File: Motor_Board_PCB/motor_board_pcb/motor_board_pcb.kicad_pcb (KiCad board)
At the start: 2 copper layers, 104.8 x 60.3 mm, 107 parts, among them J1 CAN_OUT, J11 CSP-USC16-TR, J2 Screw_Terminal_01x04, J3 Conn_01x02, J4 Screw_Terminal_01x14, J5 Screw_Terminal_01x04, J6 Conn_01x03, J8 Conn_01x02, SW1 SW_Push, U1 R7FA4M1AB3CFM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

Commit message: Motor Board Initial Layout
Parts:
- removed R7: 5.1k, Resistor_SMD:R_0603_1608Metric
- removed SW1: SW_Push, Button_Switch_SMD:SW_Push_1P1T_NO_6x6mm_H9.5mm
- removed TP1, TP4, TP6: TestPoint, TestPoint:TestPoint_Pad_D1.0mm
- added TP10: TestPoint, TestPoint:TestPoint_Pad_D1.0mm, F.Cu at (143.3, 89.7)
- added TP11: TestPoint, TestPoint:TestPoint_Pad_D1.0mm, F.Cu at (139.3, 89.7)
- added TP12: TestPoint, TestPoint:TestPoint_Pad_D1.0mm, F.Cu at (141.3, 89.7)
- added TP13: TestPoint, TestPoint:TestPoint_Pad_D1.0mm, F.Cu at (137.3, 89.7)
- added TP14: TestPoint, TestPoint:TestPoint_Pad_D1.0mm, F.Cu at (153.4, 76.8)
- added TP15: TestPoint, TestPoint:TestPoint_Pad_D1.0mm, F.Cu at (151.4, 76.8)
- added TP16: TestPoint, TestPoint:TestPoint_Pad_D1.0mm, F.Cu at (158.0, 72.8)
- added TP17: TestPoint, TestPoint:TestPoint_Pad_D1.0mm, F.Cu at (160.0, 72.8)
- C1, C4, C8, L1, L2, R22, R3: moved to F.Cu
- C31, R1, R10, R11, R13, R14, R15, R2, R30, R4, R8, R9, RV1: moved to B.Cu
- J4: value Screw_Terminal_01x14 -> Screw_Terminal_01x06; footprint Connector_PinHeader_2.54mm:PinHeader_1x14_P2.54mm_Vertical -> Connector_PinHeader_2.54mm:PinHeader_1x06_P2.54mm_Vertical
- R6: value 5.1k -> 10k
- moved J3 128.4 mm to (94.5, 65.5), turned to 180 degrees
- moved R33 122.6 mm to (135.2, 73.0), turned to 180 degrees
- moved R32 119.5 mm to (138.4, 77.8), turned to 180 degrees
- moved TP9 116.4 mm to (129.6, 83.0)
- moved R31 116.0 mm to (141.9, 74.6)
- moved R1 109.1 mm to (167.9, 69.0), turned to -90 degrees
- moved R2 101.7 mm to (173.3, 69.1), turned to -90 degrees
- moved J8 97.9 mm to (184.9, 65.3), turned to 180 degrees
- moved J6 97.8 mm to (154.2, 60.1), turned to 90 degrees
- moved TP8 90.5 mm to (174.0, 72.7)
- moved TP7 89.1 mm to (174.0, 74.9)
- moved TP2 81.0 mm to (181.7, 68.7)
- moved D11 78.1 mm to (181.8, 64.8), turned to -90 degrees
- moved J5 69.4 mm to (184.6, 101.0), turned to -90 degrees
- moved J1 49.8 mm to (95.3, 91.6), turned to 180 degrees
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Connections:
- J4 pad 2: D13 -> D5
- J4 pad 3: D12 -> D4
- J4 pad 4: D11 -> D3
- J4 pad 5: D10 -> D2
- J4 pad 6: D7 -> GND
- R31 pad 1: Net-(U4-MS1_AD0) -> Net-(U4-MS2_AD1)
- R6 pad 2: Net-(R6-Pad2) -> GND
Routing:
- net +5V: track 0.00 -> 242.7 mm, vias 0 -> 7
- net GND: track 0.00 -> 54.5 mm, vias 0 -> 53
- net +12V: track 0.00 -> 45.8 mm, vias 0 -> 14
- net D11: track 0.00 -> 42.4 mm, vias 0 -> 4
- net D12: track 0.00 -> 40.8 mm, vias 0 -> 2
- net D13: track 0.00 -> 39.6 mm, vias 0 -> 2
- net D10: track 0.00 -> 38.4 mm
- net BOOT: track 0.00 -> 33.4 mm, vias 0 -> 1
- net ~{RESET}: track 0.00 -> 32.5 mm, vias 0 -> 1
- net /Connectors/SHIELD2: track 0.00 -> 29.6 mm, vias 0 -> 1
- net Net-(D6-K): track 0.00 -> 29.5 mm, vias 0 -> 2
- net D7: track 0.00 -> 28.2 mm, vias 0 -> 2
- net Net-(D7-K): track 0.00 -> 27.8 mm, vias 0 -> 2
- net VUSB: track 0.00 -> 27.1 mm, vias 0 -> 1
- net D6: track 0.00 -> 27.0 mm, vias 0 -> 2
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- added copper zone on B.Cu, net +12V
- added copper zone on F.Cu, net +12V
- added copper zone on F.Cu, net +5V
- added copper zone on F.Cu, net -BATT
- added copper zone on F.Cu, net /Motor_Driver/OUTA1
- added copper zone on F.Cu, net /Motor_Driver/OUTA2
- added copper zone on F.Cu, net /Motor_Driver/OUTB1
- added copper zone on F.Cu, net /Motor_Driver/OUTB2
- added copper zone on B.Cu, net GND
- added copper zone on F.Cu, net GND
- added copper zone on F.Cu, net Net-(C27-Pad2)
- added copper zone on F.Cu, net Net-(C30-Pad2)
- added copper zone on F.Cu, net Net-(C32-Pad2)
- added copper zone on F.Cu, net Net-(U6-BST)
- added copper zone on F.Cu, net Net-(U6-SW)
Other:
- board size 104.8 x 60.3 mm -> 95 x 45 mm
- rule pad_to_mask_clearance: 0 -> 0.05
- board text added: "PWR"
- board text added: "RX"
- board text added: "SCK"
- board text added: "TX"

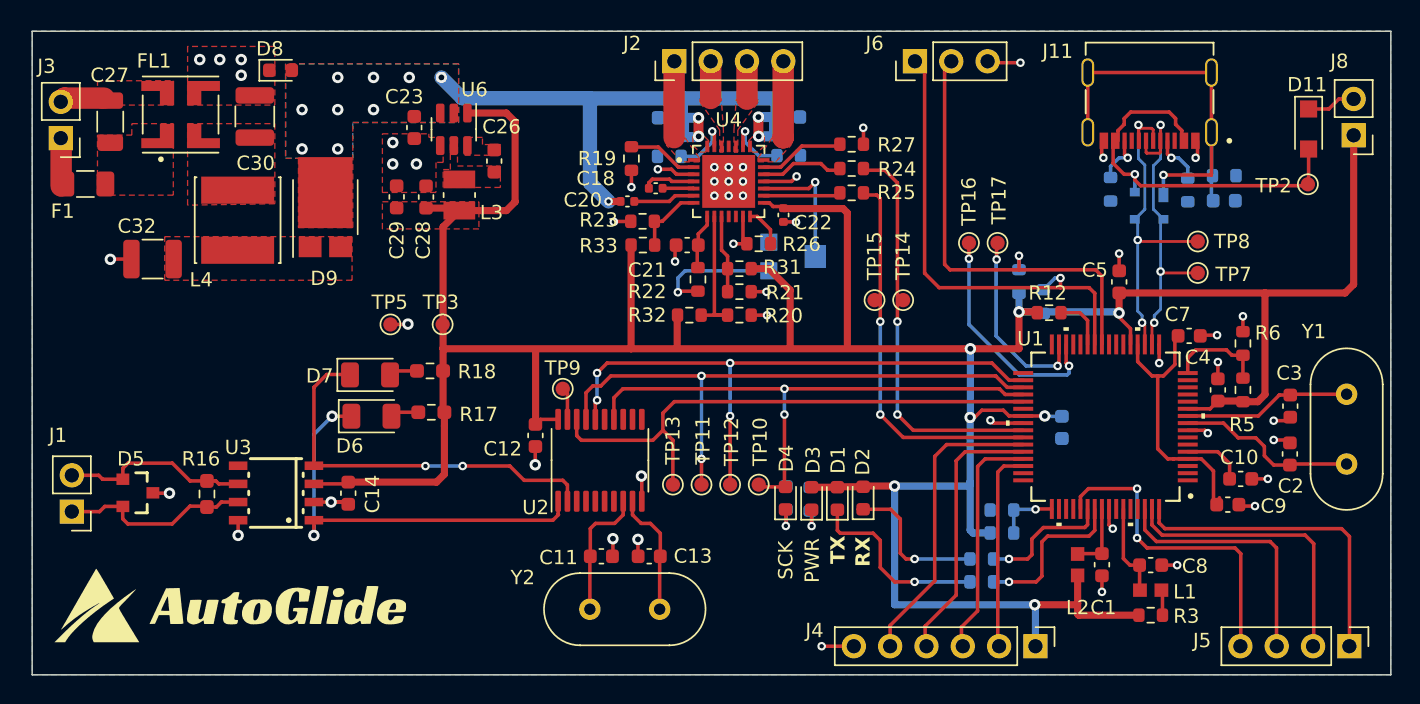
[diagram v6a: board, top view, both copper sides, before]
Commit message: Central hub layout first draft (+ some changes to motor driver)
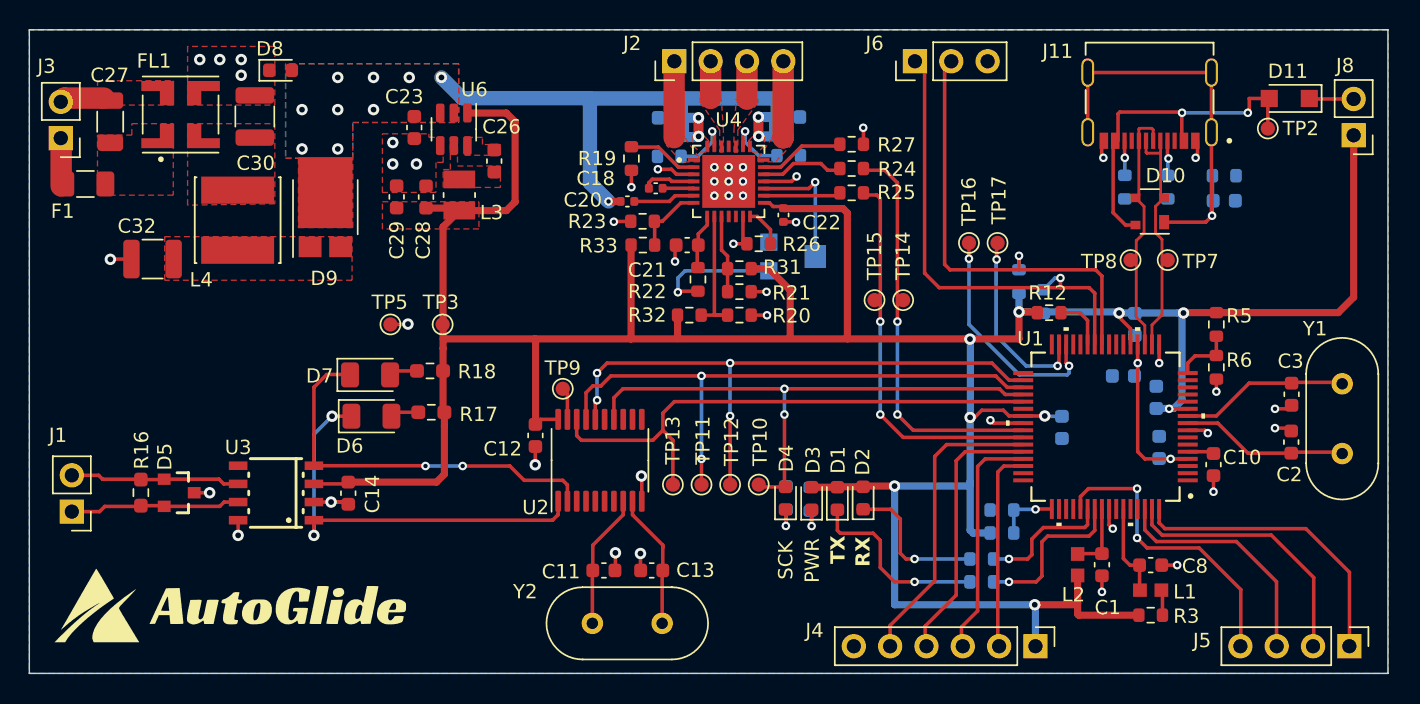
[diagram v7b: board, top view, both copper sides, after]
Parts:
- C4, C5, C7, C9: moved to B.Cu
- D10: moved to F.Cu
- moved C9 6.25 mm to (171.3, 87.1), turned to -90 degrees
- moved C7 5.39 mm to (168.8, 82.1), turned to 0 degrees
- moved R5 4.94 mm to (175.3, 78.5), turned to -90 degrees
- moved TP8 4.88 mm to (169.3, 74.0)
- moved TP2 4.80 mm to (178.9, 64.8)
- moved R16 4.62 mm to (100.1, 90.3)
- moved C4 4.34 mm to (171.1, 83.6)
- moved C5 3.17 mm to (169.6, 78.5), turned to 90 degrees
- moved D5 2.89 mm to (102.7, 90.3)
- moved D11 2.53 mm to (180.4, 62.7), turned to 180 degrees
- moved R6 2.50 mm to (175.3, 81.5), turned to -90 degrees
- moved TP7 2.28 mm to (171.9, 74.0)
- moved C10 2.15 mm to (175.1, 88.3), turned to 90 degrees
- moved R2 1.41 mm to (171.9, 68.9)
- moved R1 1.01 mm to (168.9, 68.9)
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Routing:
- net GND: track 54.5 -> 45.4 mm, vias 53 -> 47
- net USB_D+: track 24.0 -> 17.7 mm, vias 3 -> 0
- net /MCU/MCU_3V3: track 18.7 -> 12.6 mm, vias 0 -> 2
- net +5V: track 242.7 -> 237.2 mm, vias 7 -> 9
- net USB_D-: track 22.3 -> 16.9 mm, vias 3 -> 0
- net Net-(U1-P407/USB_VBUS/ADTRG0): track 6.91 -> 4.27 mm
- net VUSB: track 27.1 -> 24.5 mm, vias 1 -> 2
- net Net-(U1-VCL): track 4.34 -> 2.10 mm
- net A0: track 22.1 -> 20.6 mm
- net A1: track 21.7 -> 20.3 mm
- net /CAN/CAN_HI: track 13.4 -> 11.9 mm
- net A2: track 19.5 -> 18.1 mm
- net A3: track 17.5 -> 16.1 mm
- net /CAN/CAN_LOW: track 13.3 -> 11.9 mm
- net CC2: track 3.51 -> 2.47 mm
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
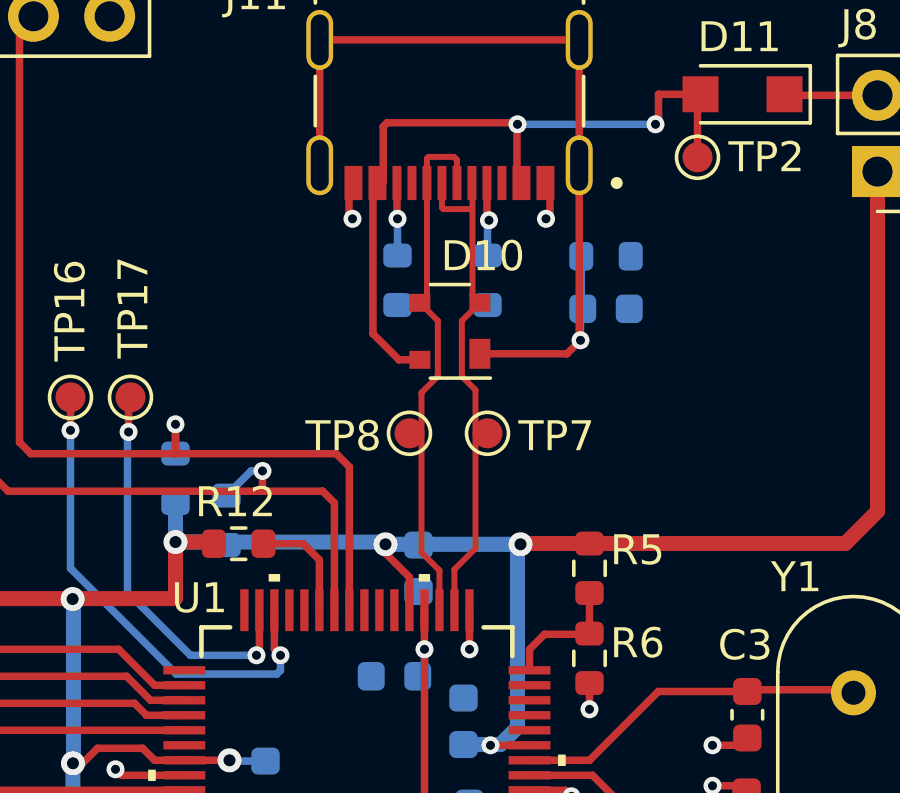
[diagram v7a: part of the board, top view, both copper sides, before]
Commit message: Small changes to USB connector d+ and d- traces
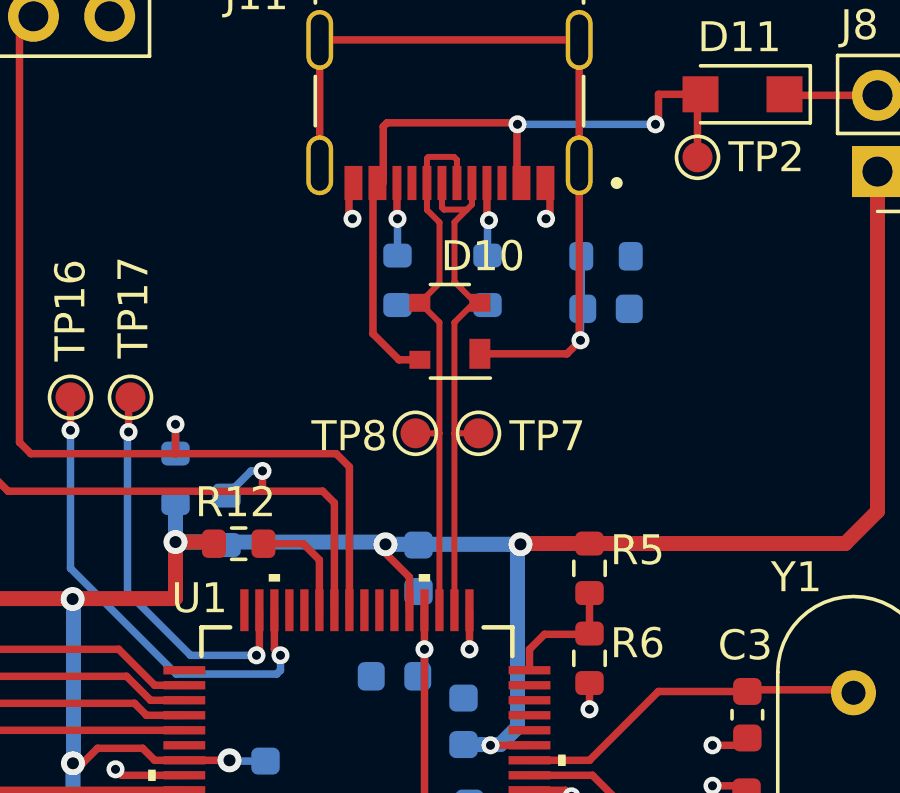
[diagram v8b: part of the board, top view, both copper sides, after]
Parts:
- moved TP7 0.30 mm to (171.6, 74.0)
- moved TP8 0.20 mm to (169.5, 74.0)
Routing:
- net USB_D-: track 16.9 -> 17.9 mm
- net USB_D+: track 17.7 -> 18.4 mm
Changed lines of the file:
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@@
   )
   (footprint "TestPoint:TestPoint_Pad_D1.0mm" (layer "F.Cu")
-    (at 171.9 74)
+    (at 171.6 74)
     (descr "SMD pad as test Point, diameter 1.0mm")
     (tags "test point SMD pad")
@@
   )
   (footprint "TestPoint:TestPoint_Pad_D1.0mm" (layer "F.Cu")
-    (at 169.3 74)
+    (at 169.5 74)
     (descr "SMD pad as test Point, diameter 1.0mm")
     (tags "test point SMD pad")
@@
   (segment (start 117.8 81.75) (end 117.522597 82.027403) (width 0.25) (layer "F.Cu") (net 32))
   (segment (start 170.382173 65.656462) (end 170.382173 66.476462) (width 0.2) (layer "F.Cu") (net 33))
-  (segment (start 171.5 72.554957) (end 171.5 77.836711) (width 0.2) (layer "F.Cu") (net 33))
-  (segment (start 171.5 77.836711) (end 170.797719 78.538992) (width 0.2) (layer "F.Cu") (net 33))
-  (segment (start 170.797719 78.538992) (end 170.797719 79.896711) (width 0.2) (layer "F.Cu") (net 33))
-  (segment (start 170.382173 66.476462) (end 170.432173 66.526462) (width 0.2) (layer "F.Cu") (net 33))
-  (segment (start 170.432173 66.526462) (end 171.332173 66.526462) (width 0.2) (layer "F.Cu") (net 33))
-  (segment (start 171.4 69.404957) (end 171.645043 69.65) (width 0.2) (layer "F.Cu") (net 33))
-  (segment (start 171.4 65.674289) (end 171.4 69.404957) (width 0.2) (layer "F.Cu") (net 33))
-  (segment (start 171.045043 70.25) (end 171.045043 72.1) (width 0.2) (layer "F.Cu") (net 33))
-  (segment (start 171.045043 72.1) (end 171.5 72.554957) (width 0.2) (layer "F.Cu") (net 33))
-  (segment (start 171.382173 65.656462) (end 171.4 65.674289) (width 0.2) (layer "F.Cu") (net 33))
-  (segment (start 171.645043 69.65) (end 171.045043 70.25) (width 0.2) (layer "F.Cu") (net 33))
+  (segment (start 171.382173 65.656462) (end 171.382173 66.376462) (width 0.2) (layer "F.Cu") (net 33))
+  (segment (start 171.6 74) (end 170.797719 74) (width 0.2) (layer "F.Cu") (net 33))
+  (segment (start 171.645043 69.65) (end 171.45 69.65) (width 0.2) (layer "F.Cu") (net 33))
+  (segment (start 171.45 69.65) (end 170.797719 70.302281) (width 0.2) (layer "F.Cu") (net 33))
+  (segment (start 170.8 68.95) (end 171.5 69.65) (width 0.2) (layer "F.Cu") (net 33))
+  (segment (start 170.382173 66.476462) (end 170.44826 66.542549) (width 0.2) (layer "F.Cu") (net 33))
+  (segment (start 171.5 69.65) (end 171.645043 69.65) (width 0.2) (layer "F.Cu") (net 33))
+  (segment (start 170.8 66.958635) (end 170.8 68.95) (width 0.2) (layer "F.Cu") (net 33))
+  (segment (start 170.44826 66.542549) (end 171.216087 66.542549) (width 0.2) (layer "F.Cu") (net 33))
+  (segment (start 170.797719 70.302281) (end 170.797719 74) (width 0.2) (layer "F.Cu") (net 33))
+  (segment (start 171.382173 66.376462) (end 170.8 66.958635) (width 0.2) (layer "F.Cu") (net 33))
+  (segment (start 170.797719 74) (end 170.797719 79.896711) (width 0.2) (layer "F.Cu") (net 33))
   (segment (start 171.4 65.638635) (end 171.382173 65.656462) (width 0.2) (layer "F.Cu") (net 33))
+  (segment (start 169.645043 69.65) (end 170.297593 70.30255) (width 0.2) (layer "F.Cu") (net 34))
   (segment (start 170.882173 65.656462) (end 170.882173 64.886462) (width 0.2) (layer "F.Cu") (net 34))
-  (segment (start 169.882173 69.41287) (end 169.645043 69.65) (width 0.2) (layer "F.Cu") (net 34))
-  (segment (start 170.245043 72.1) (end 169.7 72.645043) (width 0.2) (layer "F.Cu") (net 34))
-  (segment (start 169.7 77.972911) (end 170.297593 78.570504) (width 0.2) (layer "F.Cu") (net 34))
-  (segment (start 170.245043 70.25) (end 170.245043 72.1) (width 0.2) (layer "F.Cu") (net 34))
+  (segment (start 169.882173 66.551804) (end 170.3 66.969631) (width 0.2) (layer "F.Cu") (net 34))
   (segment (start 169.882173 64.836462) (end 169.882173 65.656462) (width 0.2) (layer "F.Cu") (net 34))
+  (segment (start 169.5 74) (end 170.297593 74) (width 0.2) (layer "F.Cu") (net 34))
   (segment (start 169.932173 64.786462) (end 169.882173 64.836462) (width 0.2) (layer "F.Cu") (net 34))
-  (segment (start 169.7 72.645043) (end 169.7 77.972911) (width 0.2) (layer "F.Cu") (net 34))
-  (segment (start 169.645043 69.65) (end 170.245043 70.25) (width 0.2) (layer "F.Cu") (net 34))
   (segment (start 170.882173 64.886462) (end 170.782173 64.786462) (width 0.2) (layer "F.Cu") (net 34))
-  (segment (start 170.297593 78.570504) (end 170.297593 79.896711) (width 0.2) (layer "F.Cu") (net 34))
-  (segment (start 169.882173 65.656462) (end 169.882173 69.41287) (width 0.2) (layer "F.Cu") (net 34))
+  (segment (start 169.882173 65.656462) (end 169.882173 66.551804) (width 0.2) (layer "F.Cu") (net 34))
+  (segment (start 170.3 66.969631) (end 170.3 68.995043) (width 0.2) (layer "F.Cu") (net 34))
+  (segment (start 170.297593 74) (end 170.297593 79.896711) (width 0.2) (layer "F.Cu") (net 34))
   (segment (start 170.782173 64.786462) (end 169.932173 64.786462) (width 0.2) (layer "F.Cu") (net 34))
+  (segment (start 170.297593 70.30255) (end 170.297593 74) (width 0.2) (layer "F.Cu") (net 34))
+  (segment (start 170.3 68.995043) (end 169.645043 69.65) (width 0.2) (layer "F.Cu") (net 34))
   (segment (start 178.9 64.8) (end 178.9 62.8) (width 0.25) (layer "F.Cu") (net 35))
   (segment (start 168.082173 70.682173) (end 168.95 71.55) (width 0.25) (layer "F.Cu") (net 35))
